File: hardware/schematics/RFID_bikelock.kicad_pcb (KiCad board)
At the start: 2 copper layers, 21 x 15.5 mm, 49 parts, among them J1 BATT_p2+, J2 USB_prog, J5 GPIO out, J6 WAKE_IN_OUT, M1 Stepper_Motor_unipolar_5pin, SW1 EN, SW2 BOOT, SW3 WAKE, U1 ULN2003, U2 ESP32-S3-WROOM-1, U3 ADPL40502AUJZ-3.3-R7, U4 MIC2288, U6 MCP73871-2CC

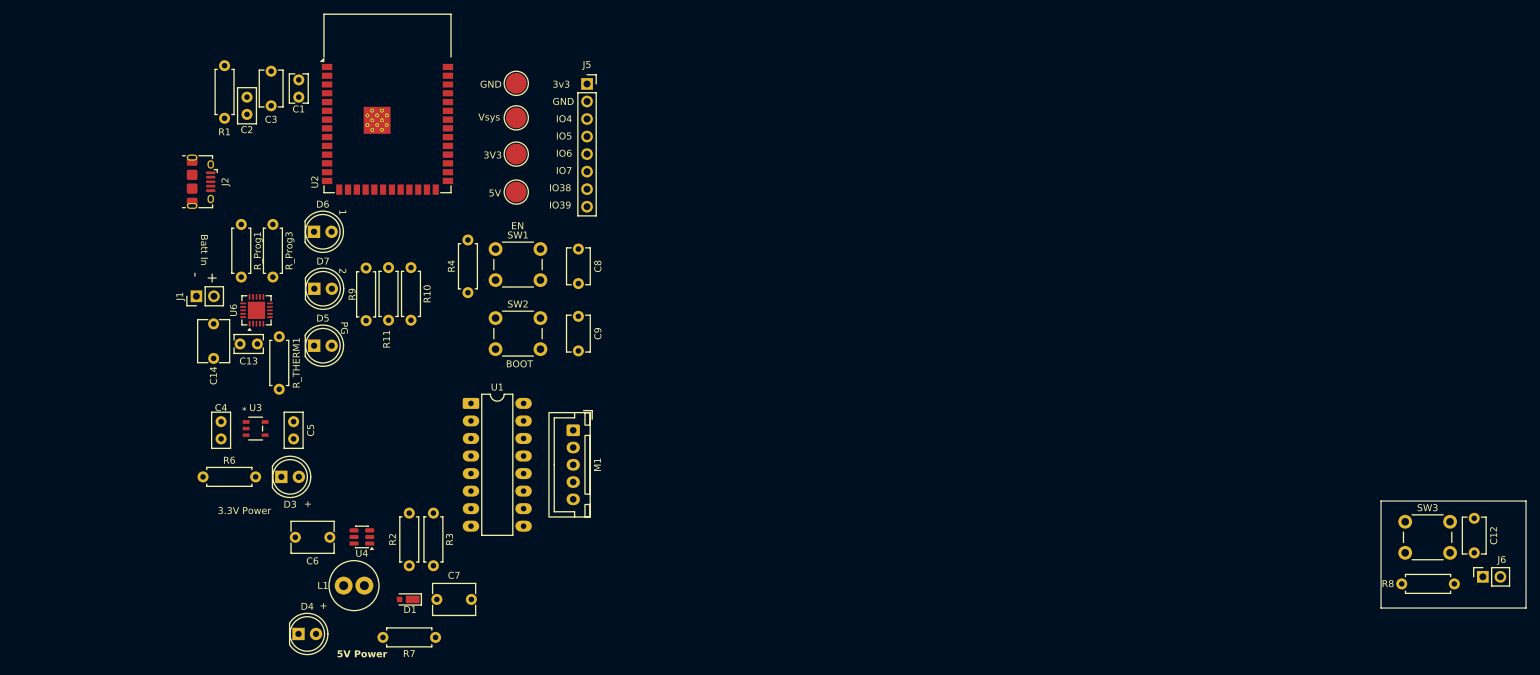
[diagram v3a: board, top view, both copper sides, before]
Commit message: Schematic changes: switched to power-path management for battery charger IC, and buck-boost converter for steady 5v DC output for motor. Also, changed all resistors/capacitors to SMD instead of THT for easier assembly.
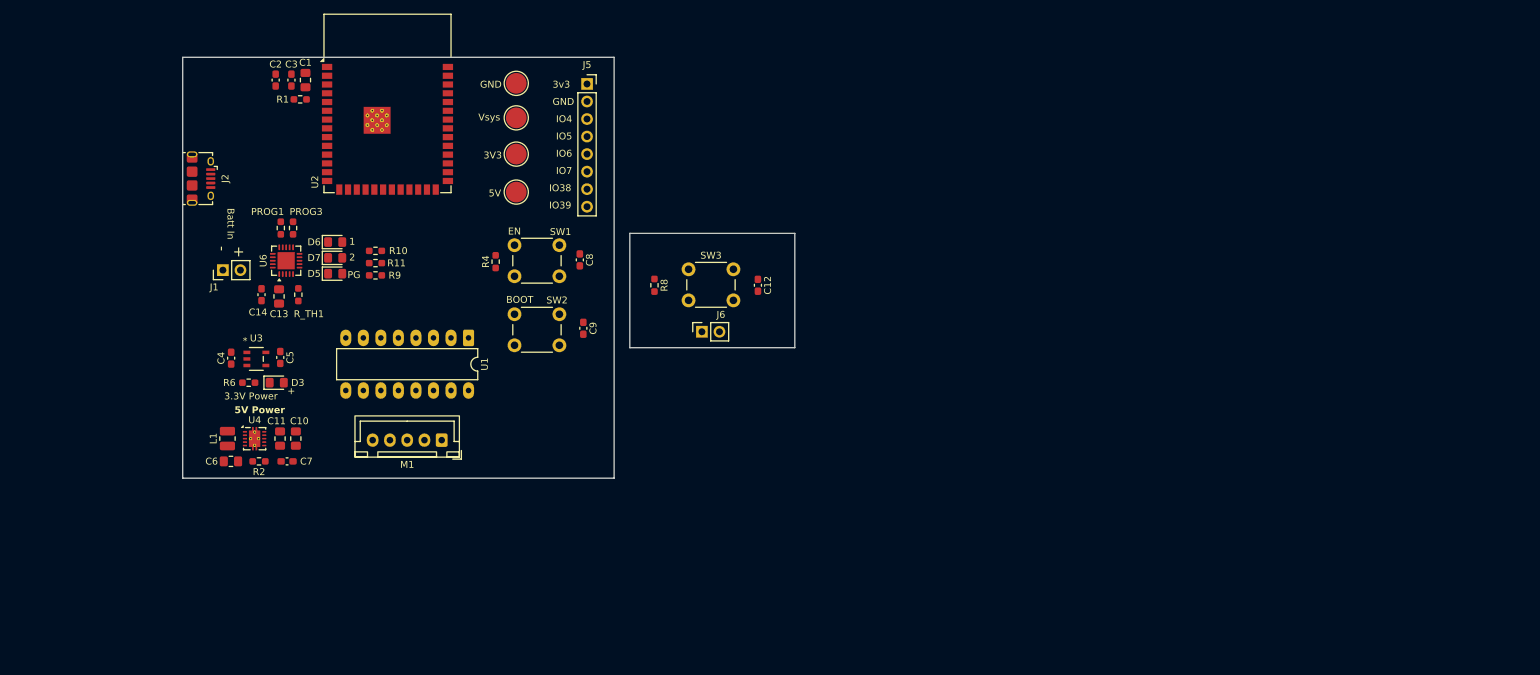
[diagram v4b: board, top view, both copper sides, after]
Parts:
- removed D1: MSS1P6, Diode_SMD:D_MicroSMP_AK
- removed D4: 5V-PWR, LED_THT:LED_D5.0mm
- removed R3: 1.87k, Resistor_THT:R_Axial_DIN0207_L6.3mm_D2.5mm_P7.62mm_Horizontal
- removed R7: 470, Resistor_THT:R_Axial_DIN0207_L6.3mm_D2.5mm_P7.62mm_Horizontal
- added C10: 10uF, Capacitor_SMD:C_0805_2012Metric_Pad1.18x1.45mm_HandSolder, F.Cu at (91.8, 133.2)
- added C11: 10uF, Capacitor_SMD:C_0805_2012Metric_Pad1.18x1.45mm_HandSolder, F.Cu at (89.5, 133.2)
- C1, C13: footprint Capacitor_THT:C_Rect_L4.0mm_W2.5mm_P2.50mm -> Capacitor_SMD:C_0805_2012Metric_Pad1.18x1.45mm_HandSolder
- C12, C3, C8, C9: footprint Capacitor_THT:C_Disc_D5.1mm_W3.2mm_P5.00mm -> Capacitor_SMD:C_0603_1608Metric_Pad1.08x0.95mm_HandSolder
- C14: footprint Capacitor_THT:C_Disc_D6.0mm_W4.4mm_P5.00mm -> Capacitor_SMD:C_0603_1608Metric_Pad1.08x0.95mm_HandSolder
- C2, C4, C5: footprint Capacitor_THT:C_Disc_D5.0mm_W2.5mm_P2.50mm -> Capacitor_SMD:C_0603_1608Metric_Pad1.08x0.95mm_HandSolder
- C6: value 4.7uF -> 10uF; footprint Capacitor_THT:C_Disc_D6.0mm_W4.4mm_P5.00mm -> Capacitor_SMD:C_0805_2012Metric_Pad1.18x1.45mm_HandSolder
- C7: value 22uF -> 0.1uF; footprint Capacitor_THT:C_Disc_D6.0mm_W4.4mm_P5.00mm -> Capacitor_SMD:C_0603_1608Metric_Pad1.08x0.95mm_HandSolder
- D3, D5, D6, D7: footprint LED_THT:LED_D5.0mm -> LED_SMD:LED_0805_2012Metric_Pad1.15x1.40mm_HandSolder
- L1: value 4.7uH -> 2.2 uH; footprint Inductor_THT:L_Radial_D7.0mm_P3.00mm -> Inductor_SMD:L_1008_2520Metric
- R1, R10, R11, R4, R6, R8, R9, R_Prog1, R_Prog3: footprint Resistor_THT:R_Axial_DIN0207_L6.3mm_D2.5mm_P7.62mm_Horizontal -> Resistor_SMD:R_0603_1608Metric_Pad0.98x0.95mm_HandSolder
- R2: value 5.62k -> 100; footprint Resistor_THT:R_Axial_DIN0207_L6.3mm_D2.5mm_P7.62mm_Horizontal -> Resistor_SMD:R_0603_1608Metric_Pad0.98x0.95mm_HandSolder
- R_TH1: renamed from R_THERM1; footprint Resistor_THT:R_Axial_DIN0207_L6.3mm_D2.5mm_P7.62mm_Horizontal -> Resistor_SMD:R_0603_1608Metric_Pad0.98x0.95mm_HandSolder
- TP1: value Batt In -> Vsys
- U4: value MIC2288 -> TPS63002; footprint Package_TO_SOT_SMD:SOT-23-6 -> Package_SON:Texas_DRC0010J_ThermalVias
- moved J6 118.5 mm to (150.6, 117.7)
- moved R8 116.6 mm to (143.8, 111.0), turned to -90 degrees
- moved SW3 110.0 mm to (148.7, 108.7)
- moved C12 109.1 mm to (158.8, 111.0)
- moved C7 29.5 mm to (90.6, 136.5)
- moved L1 27.1 mm to (81.9, 133.2), turned to -90 degrees
- moved R2 26.5 mm to (86.5, 136.5), turned to 0 degrees
- moved U4 21.1 mm to (85.9, 133.2), turned to 0 degrees
- moved M1 19.1 mm to (113.0, 133.4), turned to 180 degrees
- moved C6 18.1 mm to (82.4, 136.5)
- moved R6 15.2 mm to (85.0, 125.1)
- moved R_TH1 14.0 mm to (92.2, 112.4)
- moved D3 13.7 mm to (89.1, 125.1)
- moved R1 12.0 mm to (92.5, 84.1), turned to 0 degrees
- moved D5 10.9 mm to (97.5, 109.3)
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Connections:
- C7 pad 1: +5V -> Net-(U4-PS/SYNC)
- L1 pad 1: /Vsys -> Net-(U4-L2)
- L1 pad 2: Net-(D1-A) -> Net-(U4-L1)
- R2 pad 1: +5V -> /Vsys
- R2 pad 2: Net-(U4-FB) -> Net-(U4-PS/SYNC)
- U4 pad 1: Net-(D1-A) -> +5V
- U4 pad 2: GND -> Net-(U4-L2)
- U4 pad 3: Net-(U4-FB) -> GND
- U4 pad 4: /Boost_EN -> Net-(U4-L1)
- U4 pad 6: unconnected-(U4-NC-Pad6) -> /Boost_EN
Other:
- board size 21 x 15.5 mm -> 88.7 x 61 mm
- board text added: "PROG1"
- board text added: "PROG3"

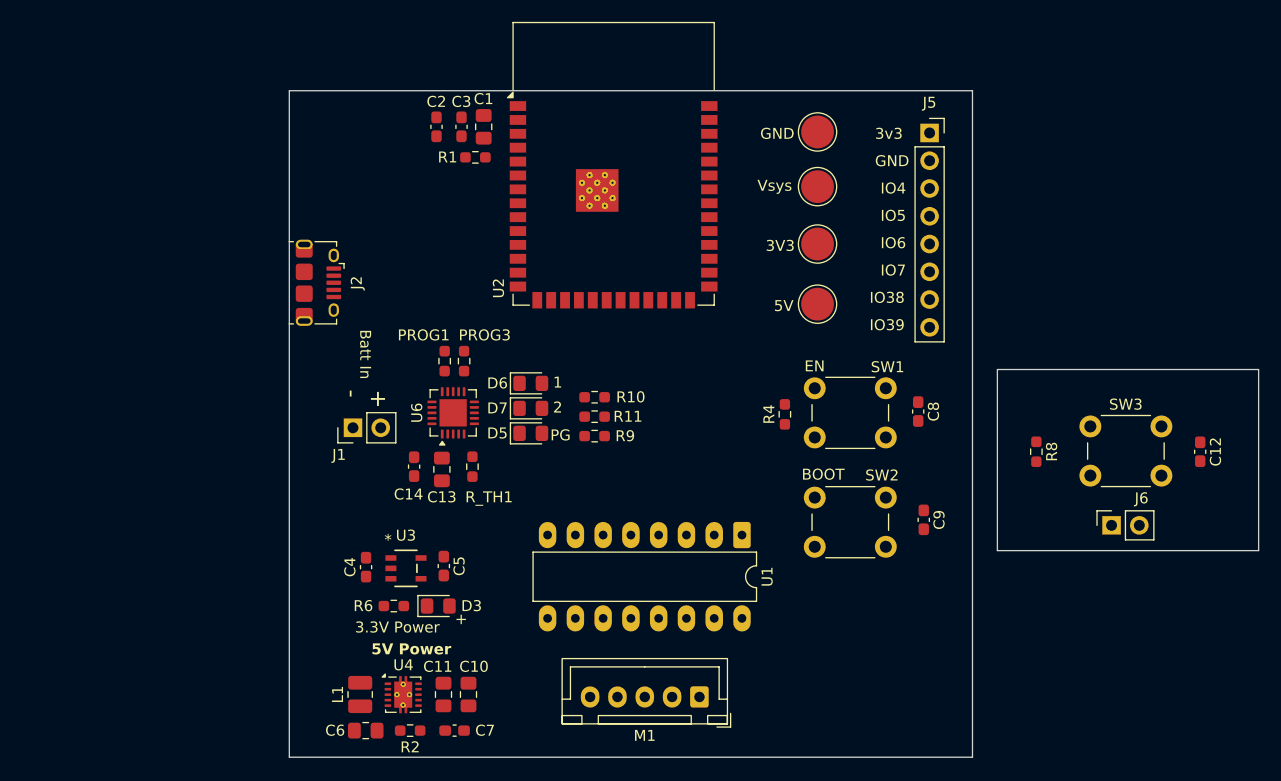
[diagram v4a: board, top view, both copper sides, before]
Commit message: Final footprint placements BEFORE routing. Commiting just in case routing has errors and we need to move things around. Added mousebite breakaway board for wakeup button.
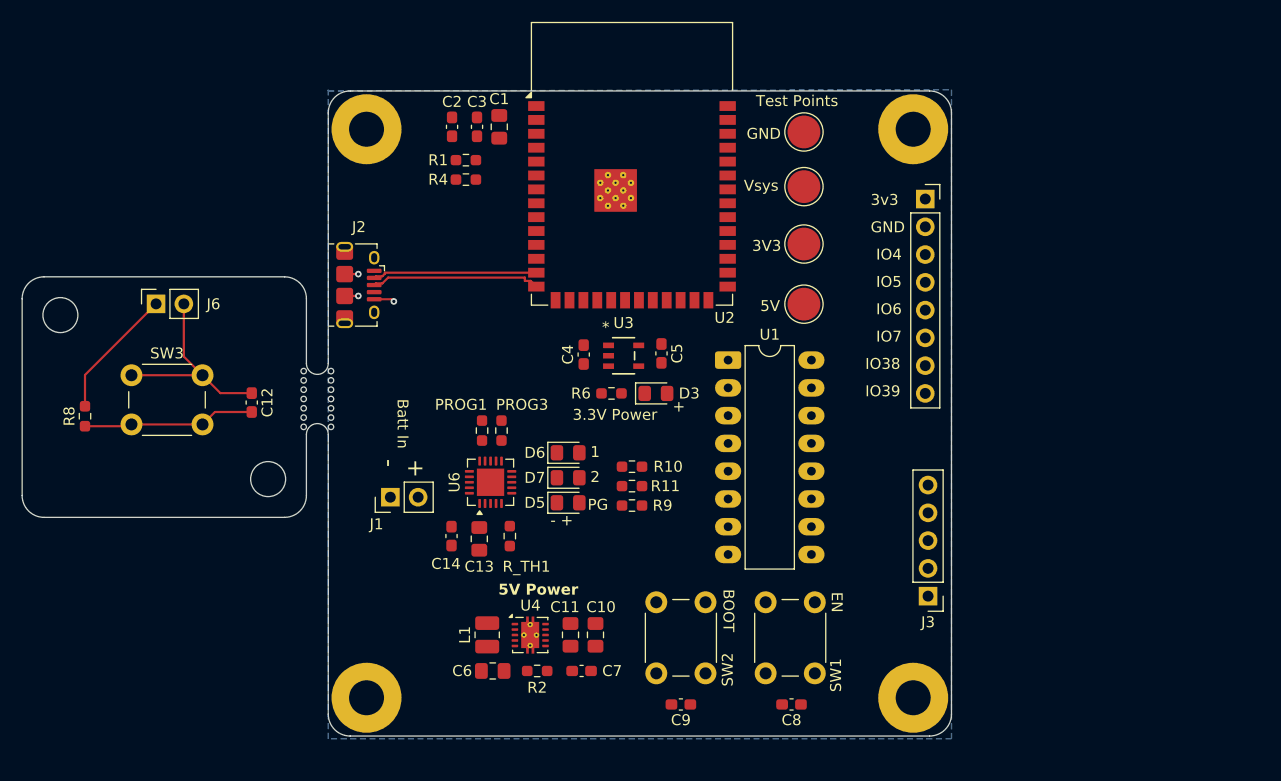
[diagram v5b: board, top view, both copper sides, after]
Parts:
- removed M1: Stepper_Motor_unipolar_5pin, Connector_JST:JST_XH_B5B-XH-A_1x05_P2.50mm_Vertical
- added H1: MountingHole_Pad, MountingHole:MountingHole_3.2mm_M3_Pad, F.Cu at (82.5, 81.5)
- added H2: MountingHole_Pad, MountingHole:MountingHole_3.2mm_M3_Pad, F.Cu at (132.5, 133.5)
- added H3: MountingHole_Pad, MountingHole:MountingHole_3.2mm_M3_Pad, F.Cu at (132.5, 81.5)
- added H4: MountingHole_Pad, MountingHole:MountingHole_3.2mm_M3_Pad, F.Cu at (82.5, 133.5)
- added H5: MountingHole, MountingHole:MountingHole_3.2mm_M3, F.Cu at (54.5, 98.5)
- added H6: MountingHole, MountingHole:MountingHole_3.2mm_M3, F.Cu at (73.5, 113.5)
- added J3: motor_out, Connector_PinHeader_2.54mm:PinHeader_1x05_P2.54mm_Vertical, F.Cu at (133.9, 124.2)
- added REF**: MouseBite-Slot_2.0x4.5mm_inset_D0.5mm_P0.85mm_7h, Panelization:MouseBite-Slot_2.0x4.5mm_inset_D0.5mm_P0.85mm_7h, F.Cu at (79.0, 106.2)
- moved J6 89.7 mm to (63.2, 97.5)
- moved SW3 87.8 mm to (61.0, 104.0)
- moved R8 87.1 mm to (56.8, 107.8), turned to 90 degrees
- moved C12 86.9 mm to (72.0, 106.5)
- moved R4 36.2 mm to (91.6, 86.1), turned to 0 degrees
- moved C8 29.2 mm to (121.4, 134.1), turned to 180 degrees
- moved C9 27.9 mm to (111.3, 134.1), turned to 180 degrees
- moved C5 27.8 mm to (109.5, 102.0)
- moved R6 27.8 mm to (104.9, 105.7)
- moved U3 27.8 mm to (106.0, 102.2)
- moved C4 27.8 mm to (102.4, 102.1)
- moved D3 27.8 mm to (109.0, 105.7)
- moved SW1 19.6 mm to (123.5, 124.8), turned to -90 degrees
- moved U1 16.1 mm to (115.6, 102.6), turned to 0 degrees
- moved SW2 13.8 mm to (113.5, 124.8), turned to -90 degrees
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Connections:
- U1 pad 14: +5V -> Net-(J3-Pin_3)
- U1 pad 15: +5V -> Net-(J3-Pin_4)
- U1 pad 16: +5V -> Net-(J3-Pin_5)
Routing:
- net Net-(J6-Pin_2): track 0.00 -> 18.9 mm
- net Net-(C12-Pad2): track 0.00 -> 15.8 mm
- net /USB-D+: track 0.00 -> 15.6 mm
- net /USB-D-: track 0.00 -> 15.1 mm
- net Net-(J6-Pin_1): track 0.00 -> 12.1 mm
- net GND: track 0.00 -> 4.38 mm, vias 0 -> 3
- added copper zone on B.Cu, net GND
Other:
- board size 88.7 x 61 mm -> 85 x 59 mm
- board text added: "- +"
- board text added: "Test Points"

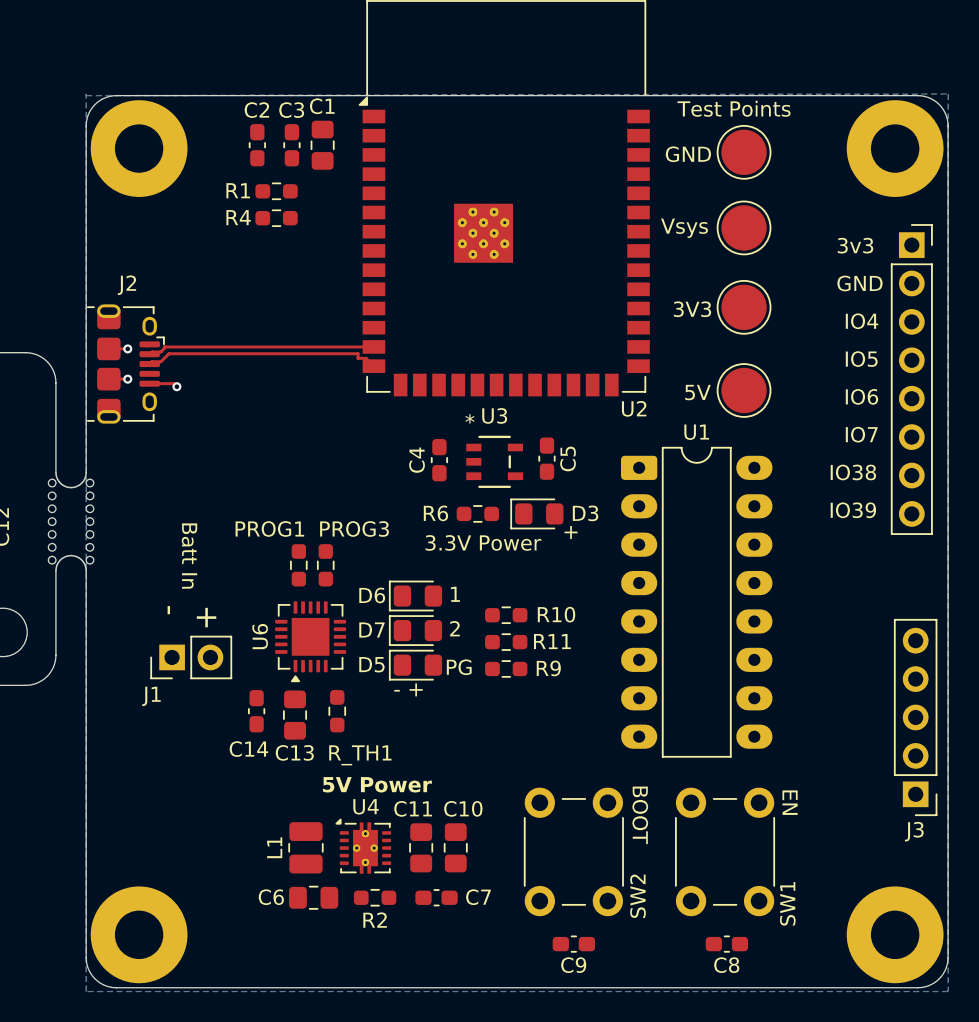
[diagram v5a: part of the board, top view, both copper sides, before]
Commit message: Final routing done, DRC clear
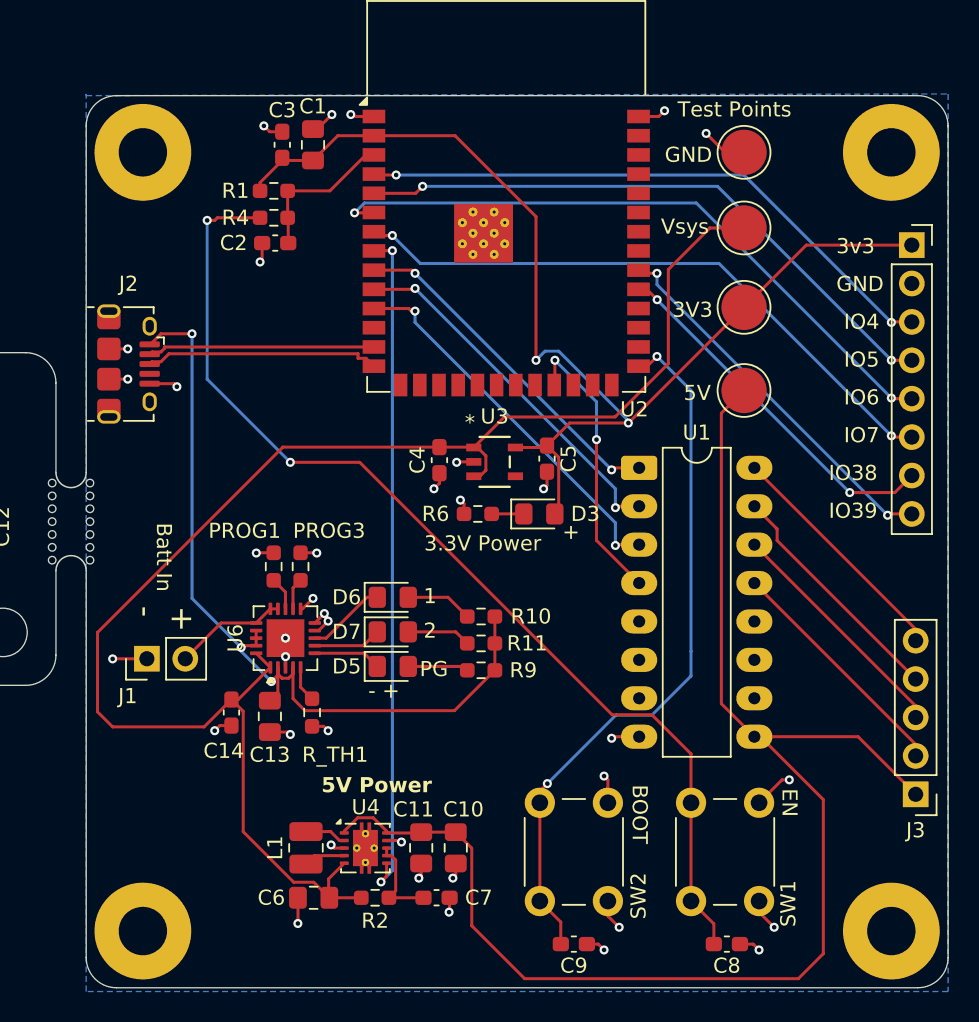
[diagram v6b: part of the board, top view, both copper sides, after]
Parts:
- moved C2 6.58 mm to (91.5, 87.8), turned to 180 degrees
- moved C13 1.67 mm to (91.1, 119.1)
- moved J1 1.67 mm to (83.0, 115.2)
- moved R9 1.67 mm to (105.1, 116.0)
- moved C14 1.67 mm to (88.6, 118.8)
- moved R10 1.67 mm to (105.1, 112.4)
- moved R11 1.67 mm to (105.1, 114.2)
- moved R_Prog1 1.67 mm to (91.4, 109.1)
- moved R_Prog3 1.67 mm to (93.2, 109.1)
- moved R_TH1 1.67 mm to (93.9, 118.8)
- moved U6 1.67 mm to (92.2, 113.9)
- moved D5 1.67 mm to (99.3, 115.8)
- moved D6 1.67 mm to (99.3, 111.2)
- moved D7 1.67 mm to (99.3, 113.5)
- moved C1 0.64 mm to (94.0, 81.2)
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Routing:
- net /Vsys: track 0.00 -> 101.9 mm
- net +5V: track 0.00 -> 93.5 mm
- net +3V3: track 0.00 -> 77.2 mm, vias 0 -> 2
- net Net-(C8-Pad2): track 0.00 -> 69.5 mm, vias 0 -> 2
- net /Vin: track 0.00 -> 56.3 mm, vias 0 -> 3
- net GND: track 4.38 -> 52.0 mm, vias 3 -> 37
- net /BOOT: track 0.00 -> 47.4 mm, vias 0 -> 2
- net /Boost_EN: track 0.00 -> 44.7 mm, vias 0 -> 2
- net /IO6: track 0.00 -> 43.8 mm, vias 0 -> 2
- net /IO7: track 0.00 -> 41.2 mm, vias 0 -> 2
- net /IO5: track 0.00 -> 40.5 mm, vias 0 -> 2
- net /IO4: track 0.00 -> 39.7 mm, vias 0 -> 2
- net /STEP3: track 0.00 -> 25.4 mm, vias 0 -> 2
- net /IO39: track 0.00 -> 25.3 mm, vias 0 -> 2
- net /STEP2: track 0.00 -> 24.3 mm, vias 0 -> 2
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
